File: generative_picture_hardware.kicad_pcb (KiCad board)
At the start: 2 copper layers, 100 x 100 mm, 59 parts, among them J1 e_Paper_HAT, J2 Conn_ARM_JTAG_SWD_10, J3 USB_C_Receptacle_USB2.0, Q1 PMN48XP, Q2 DMG9926UDM, Q3 MBT3904DW1, SW1 SW_Push, SW2 SW_Push, U1 AP2112K-3.3, U2 ESP32-WROOM-32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

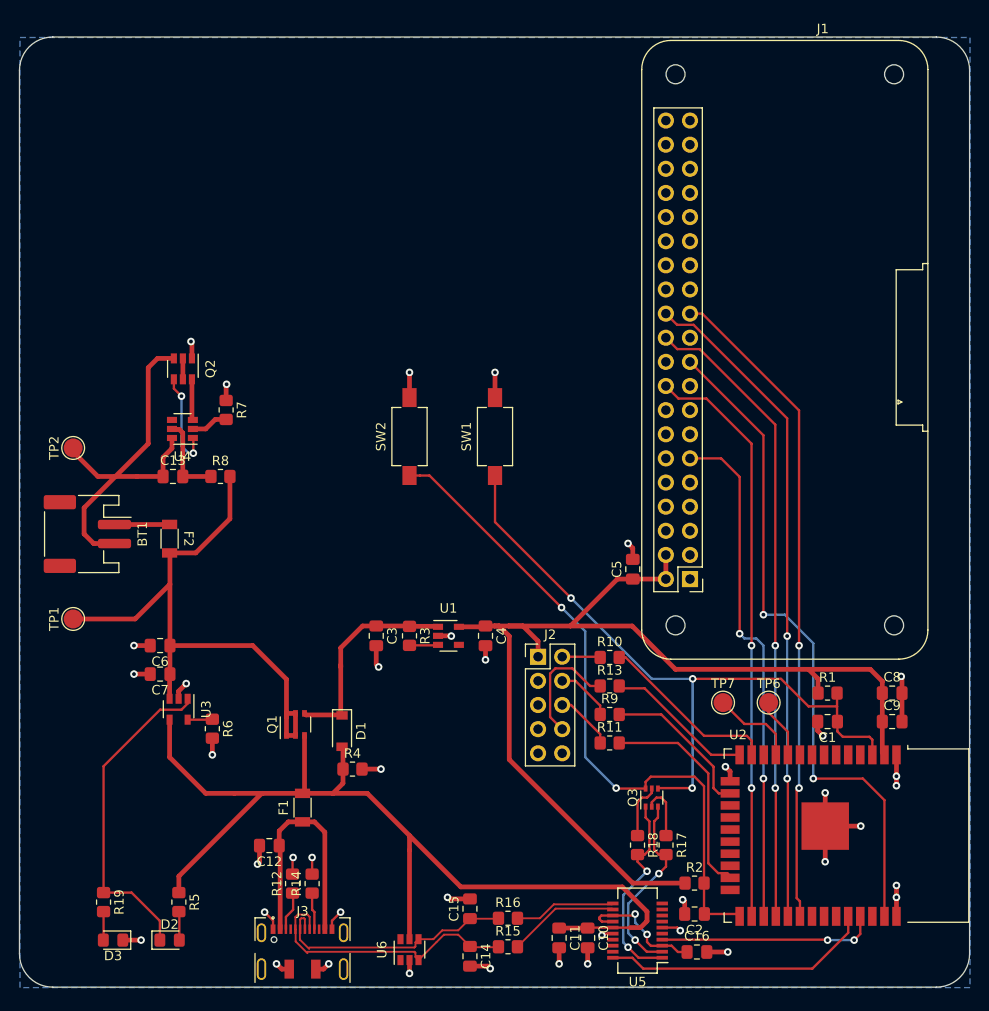
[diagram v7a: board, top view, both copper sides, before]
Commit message: Organizes silkscreen a bit
This is not final, but it removes the silkscreen related DRC errors.
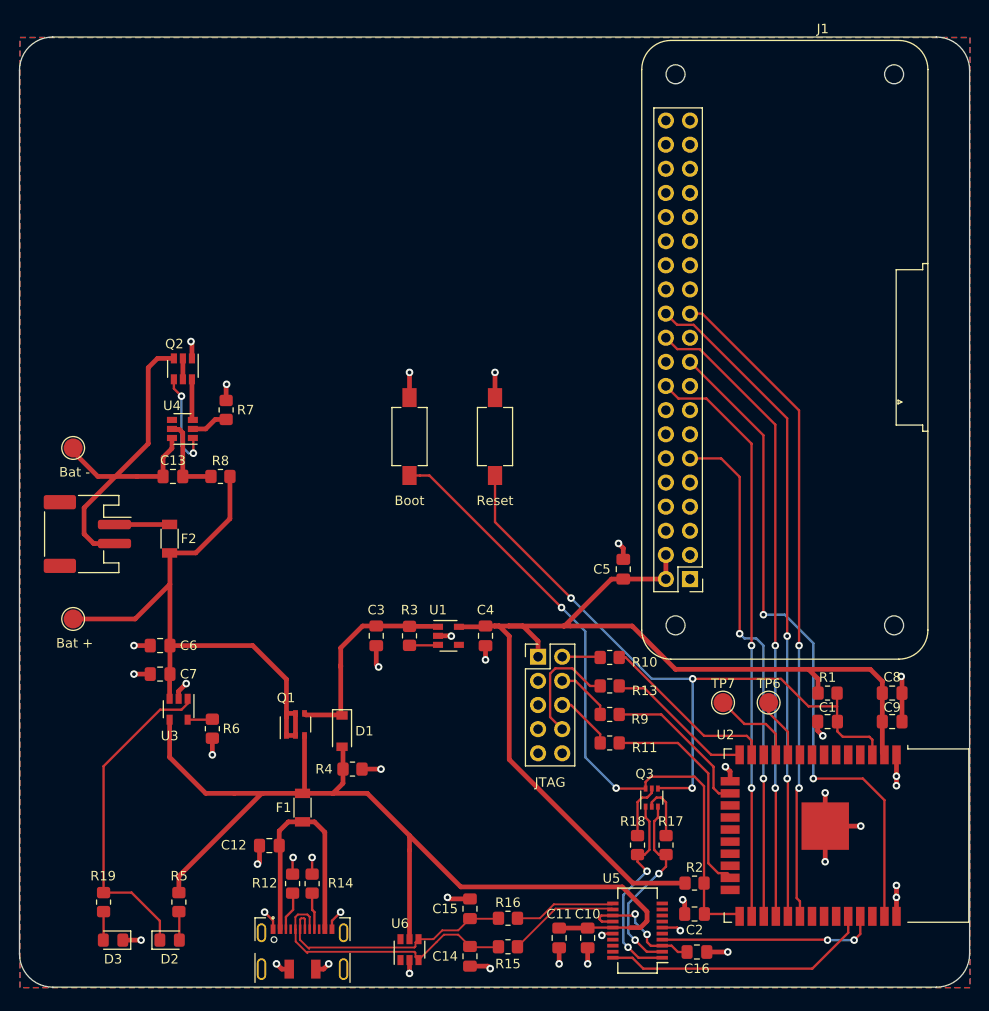
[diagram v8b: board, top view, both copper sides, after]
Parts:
- Bat +: renamed from TP1
- Bat -: renamed from TP2
- moved C5 1.00 mm to (163.5, 108.0)
- renumbered SW2 to Boot, J2 to JTAG, SW1 to Reset
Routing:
- net +3V3: track 116.7 -> 117.4 mm
- added copper zone on F.Cu, net GND
